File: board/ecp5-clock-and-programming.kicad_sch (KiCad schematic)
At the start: 32 parts

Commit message: Add metadata
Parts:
- removed 5V_LINE1: Conn_01x02_Socket, Connector_PinSocket_2.54mm:PinSocket_1x02_P2.54mm_Vertical, symbol Connector:Conn_01x02_Socket
- removed C1, C3, C4, C5, C6: 10uF, Capacitor_SMD:C_0603_1608Metric, symbol Device:C
- removed C10, C11, C13, C2, C7, C8: 100nF, Capacitor_SMD:C_0402_1005Metric, symbol Device:C
- removed C12, C15, C9: 10nF, Capacitor_SMD:C_0402_1005Metric, symbol Device:C
- removed C14, C17: 22uF, Capacitor_SMD:C_0603_1608Metric, symbol Device:C
- removed C16, C20: 1uF, Capacitor_SMD:C_0402_1005Metric, symbol Device:C
- removed C18, C19: 1nF, Capacitor_SMD:C_0402_1005Metric, symbol Device:C
- removed FPGA1: LFE5U-25F, Package_BGA:Lattice_caBGA-381_17.0x17.0mm_Layout20x20_P0.8mm_Ball0.4mm_Pad0.4mm_NSMD, symbol FPGA_Lattice:LFE5U-85F-8BG381x
- removed L1, L2: 2.2uH, Inductor_SMD:L_0805_2012Metric, symbol Device:L
- removed LDO_REG1: TLV73325PDBVR, Package_TO_SOT_SMD:SOT-23-5, symbol Regulator_Linear:TLV73325PDBV
- removed R1: 100R, Resistor_SMD:R_0402_1005Metric, symbol Device:R
- removed R2: 10K, Resistor_SMD:R_0402_1005Metric, symbol Device:R
- removed R3: 12K, Resistor_SMD:R_0402_1005Metric, symbol Device:R
- removed SW_REG1: TPS63001DRCR, Package_SON:Texas_DRC0010J_ThermalVias, symbol Regulator_Switching:TPS63001
- removed SW_REG2: TPS565208, Package_TO_SOT_SMD:SOT-23-6, symbol Regulator_Switching:TPS565208
- removed TP1, TP2: TEST, TestPoint:TestPoint_Pad_D1.0mm, symbol Connector:TestPoint
- added BLED1, BLED2: LED, LED_SMD:LED_0603_1608Metric, symbol Device:LED
- added BOOT_BTN1: SW_Push, Button_Switch_THT:SW_PUSH_6mm, symbol Switch:SW_Push
- added C45, C46: 100nF, Capacitor_SMD:C_0402_1005Metric, symbol Device:C
- added CLK1: ASEDV-16.000MHZ-LR-T, Oscillator:Oscillator_SMD_Abracon_ASE-4Pin_3.2x2.5mm, symbol Oscillator:ASE-xxxMHz
- added FLASH1: W25Q128JVS, Package_SO:SOIC-8_5.23x5.23mm_P1.27mm, symbol Memory_Flash:W25Q128JVS
- added FPGA1: LFE5U-25F, Package_BGA:Lattice_caBGA-381_17.0x17.0mm_Layout20x20_P0.8mm_Ball0.4mm_Pad0.4mm_NSMD, symbol FPGA_Lattice:LFE5U-85F-8BG381x
- added R29, R30, R32, R33, R34: 4.7K, Resistor_SMD:R_0402_1005Metric, symbol Device:R
- added R31: 10K, Resistor_SMD:R_0402_1005Metric, symbol Device:R
- added TP3: TEST, TestPoint:TestPoint_Pad_D1.0mm, symbol Connector:TestPoint
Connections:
- net +3V3: now also C45.1, C46.1, CLK1.1 (EN), CLK1.4 (Vdd), FLASH1.8 (VCC), R30.1, R31.1, R32.1
- net GND: now also BLED1.1 (K), BLED2.1 (K), BOOT_BTN1.1, C45.2, C46.2, CLK1.2 (GND), FLASH1.4 (GND), R33.2, R34.2
- new net: BLED1.2 (A), R29.2
- new net: FPGA1.R4 (CFG_2), FPGA1.U4 (CFG_0), R33.1
- new net: BLED2.2 (A), R30.2
- new net: FPGA1.T4 (CFG_1), R32.2
- new net: FPGA1.Y3 (DONE), R29.1
- new net CLK_16MHz: CLK1.3 (OUT)
- new net CSSPIN: FLASH1.1 (~{CS})
- new net IO2: FLASH1.3 (IO2)
- new net IO3: FLASH1.7 (IO3)
- new net MISO: FLASH1.2 (DO(IO1))
- new net MOSI: FLASH1.5 (DI(IO0))
- new net PROGRAMN: BOOT_BTN1.2, FPGA1.W3 (~{PROGRAM}), R31.2, TP3.1
- new net SCK: FLASH1.6 (CLK), FPGA1.U3 (CCLK)
- new net TCK: FPGA1.T5 (TCK), R34.1
- new net TDI: FPGA1.R5 (TDI)
- new net TDO: FPGA1.V4 (TDO)
- new net TMS: FPGA1.U5 (TMS)
- no-connect marks 0 -> 1
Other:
- note added: "Bootloader Button"
- note added: "ECP5 Hardware Checklist recommends using a pull-up on the pin INIT if the FPGA will be using it to handshake with other devices. However, this pin will not be used and should not need an external pull-up."
- note added: "SPI Configuration Flash"
- note added: "Select SPI Master Configuration Mode by setting CFG[2:0] == 3'b010"
- note added: "Status and Power LEDs"
- note added: "System Clock"
- note removed: "0.6V"
- note removed: "1.1 Volt Switching Regulator"
- note removed: "2.5 Volt LDO Regulator"
- note removed: "3.3 Volt Switching Regulator"
- note removed: "FPGA Power Supply Connections and Decoupling"
- note removed: "Following Ohm's and Kirchoff's laws: R22/R23 = (SW/VFB)-1"
- title: HispalisFPGA Power -> HispalisFPGA ECP5 Clock and Programming

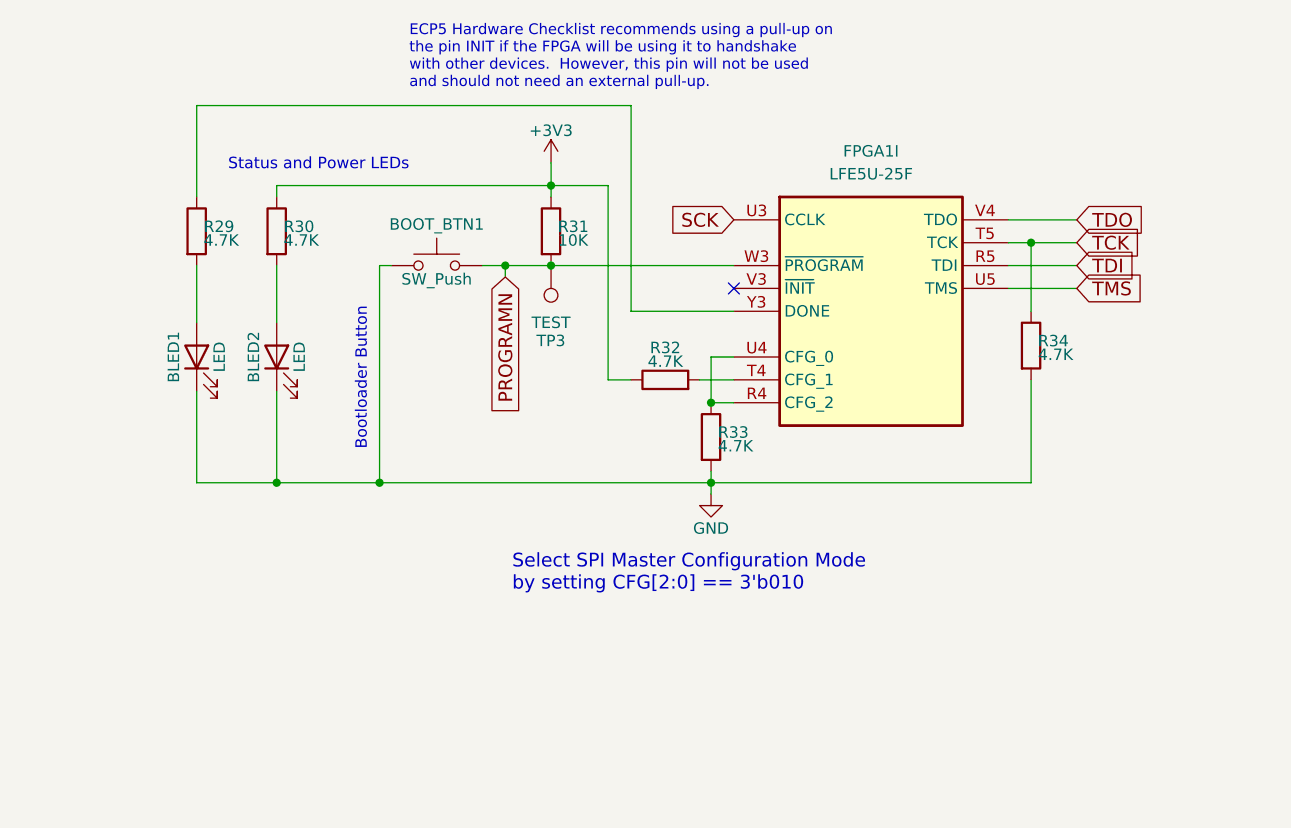
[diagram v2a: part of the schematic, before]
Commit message: Change LFE5U chip from BGA381 to BGA256 package
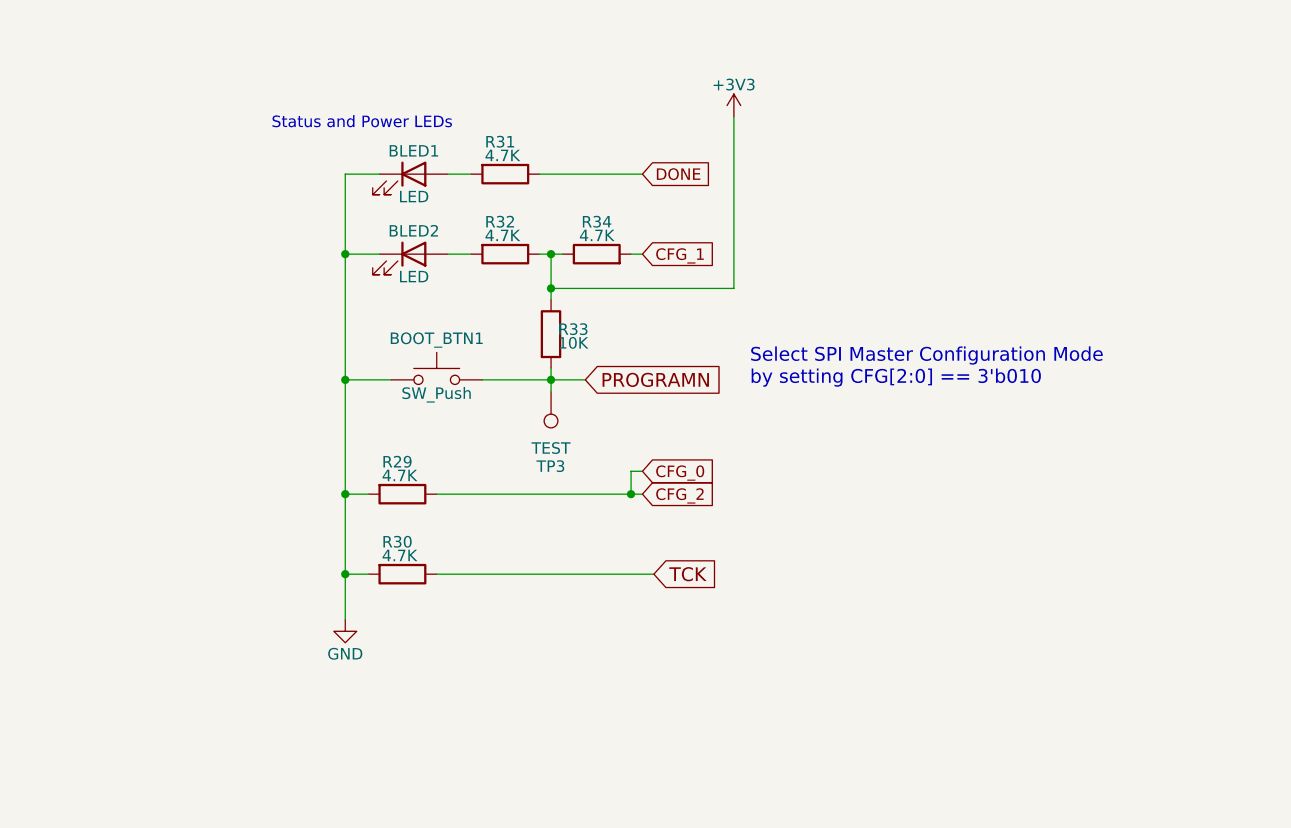
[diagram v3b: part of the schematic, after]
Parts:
- removed FPGA1: LFE5U-25F, Package_BGA:Lattice_caBGA-381_17.0x17.0mm_Layout20x20_P0.8mm_Ball0.4mm_Pad0.4mm_NSMD, symbol FPGA_Lattice:LFE5U-85F-8BG381x
- R31: value 10K -> 4.7K; LCSC C25744 -> C25900
- R33: value 4.7K -> 10K; LCSC C25900 -> C25744
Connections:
- net +3V3: now also R33.1, R34.1; no longer R30.1, R31.1
- net GND: now also R29.2, R30.2; no longer R33.2, R34.2
- net PROGRAMN: now also R33.2; no longer R31.2
- net TCK: now also R30.1; no longer R34.1
- net at BLED1.2 (A): now also R31.2; no longer R29.2
- net at BLED2.2 (A): now also R32.2; no longer R30.2
- net CFG_0: now reaches R29.1
- new net CFG_1: R34.2
- new net DONE: R31.1
- no-connect marks 1 -> 0
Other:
- note removed: "Bootloader Button"
- note removed: "ECP5 Hardware Checklist recommends using a pull-up on the pin INIT if the FPGA will be using it to handshake with other devices. However, this pin will not be used and should not need an external pull-up."
